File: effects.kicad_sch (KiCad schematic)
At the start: 0 parts

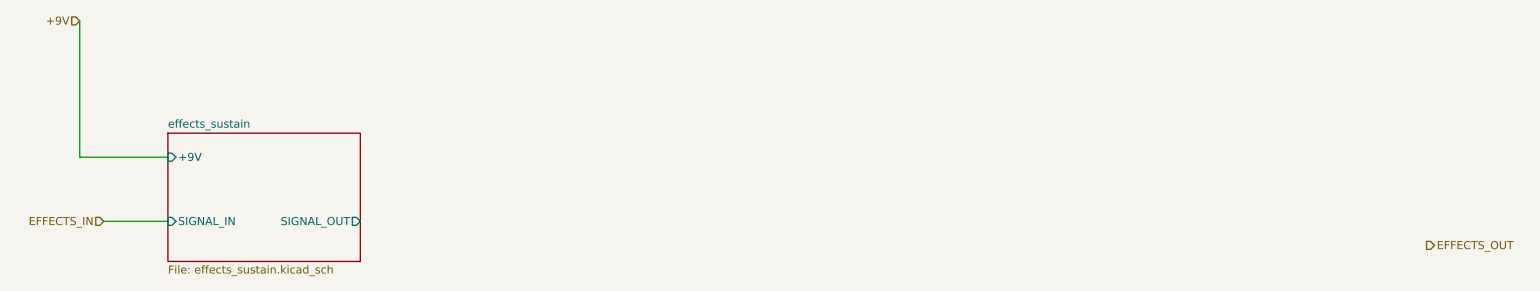
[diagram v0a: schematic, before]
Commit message: added LTSpice standard diode library to SPICE sim library, copied and simulated envelope effect, WIP determining if isolated or chained sim behaviour is correct
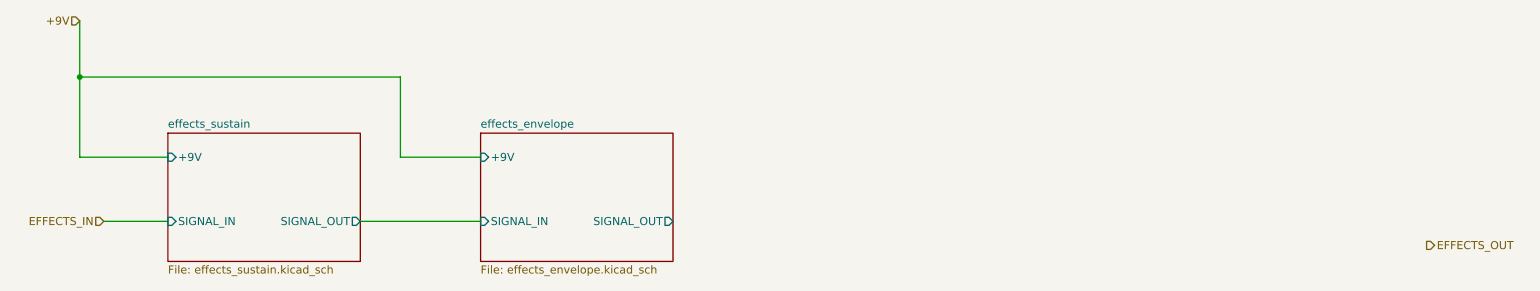
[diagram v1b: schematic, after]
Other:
- added sheet effects_envelope (effects_envelope.kicad_sch)
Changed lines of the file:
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@@
     (rev "V0.1")
   )
+  (junction (at 36.83 67.31) (diameter 0) (color 0 0 0 0)
+  )
+  (wire (pts (xy 81.28 90.17) (xy 100.33 90.17))
+    (stroke (width 0) (type default) (color 0 0 0 0))
+  )
   (wire (pts (xy 36.83 80.01) (xy 50.8 80.01))
+    (stroke (width 0) (type default) (color 0 0 0 0))
+  )
+  (wire (pts (xy 87.63 80.01) (xy 87.63 67.31))
+    (stroke (width 0) (type default) (color 0 0 0 0))
+  )
+  (wire (pts (xy 36.83 67.31) (xy 36.83 80.01))
     (stroke (width 0) (type default) (color 0 0 0 0))
   )
@@
     (stroke (width 0) (type default) (color 0 0 0 0))
   )
-  (wire (pts (xy 36.83 58.42) (xy 36.83 80.01))
+  (wire (pts (xy 36.83 58.42) (xy 36.83 67.31))
+    (stroke (width 0) (type default) (color 0 0 0 0))
+  )
+  (wire (pts (xy 100.33 80.01) (xy 87.63 80.01))
+    (stroke (width 0) (type default) (color 0 0 0 0))
+  )
+  (wire (pts (xy 87.63 67.31) (xy 36.83 67.31))
     (stroke (width 0) (type default) (color 0 0 0 0))
   )
@@
     )
   )
+  (sheet (at 100.33 76.2) (size 30.48 20.32) (fields_autoplaced)
+    (stroke (width 0.1524) (type solid) (color 0 0 0 0))
+    (fill (color 0 0 0 0.0000))
+    (property "Sheet name" "effects_envelope" (id 0) (at 100.33 75.4884 0)
+      (effects (font (size 1.27 1.27)) (justify left bottom))
+    )
+    (property "Sheet file" "effects_envelope.kicad_sch" (id 1) (at 100.33 97.1046 0)
+      (effects (font (size 1.27 1.27)) (justify left top))
+    )
+    (pin "+9V" input (at 100.33 80.01 180)
+      (effects (font (size 1.27 1.27)) (justify left))
+    )
+    (pin "SIGNAL_OUT" output (at 130.81 90.17 0)
+      (effects (font (size 1.27 1.27)) (justify right))
+    )
+    (pin "SIGNAL_IN" input (at 100.33 90.17 180)
+      (effects (font (size 1.27 1.27)) (justify left))
+    )
+  )
